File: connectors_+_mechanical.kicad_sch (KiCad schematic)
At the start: 6 parts, among them J1 Conn_01x06, J2 Conn_01x06, J3 Conn_01x04, Q1 BSP613P

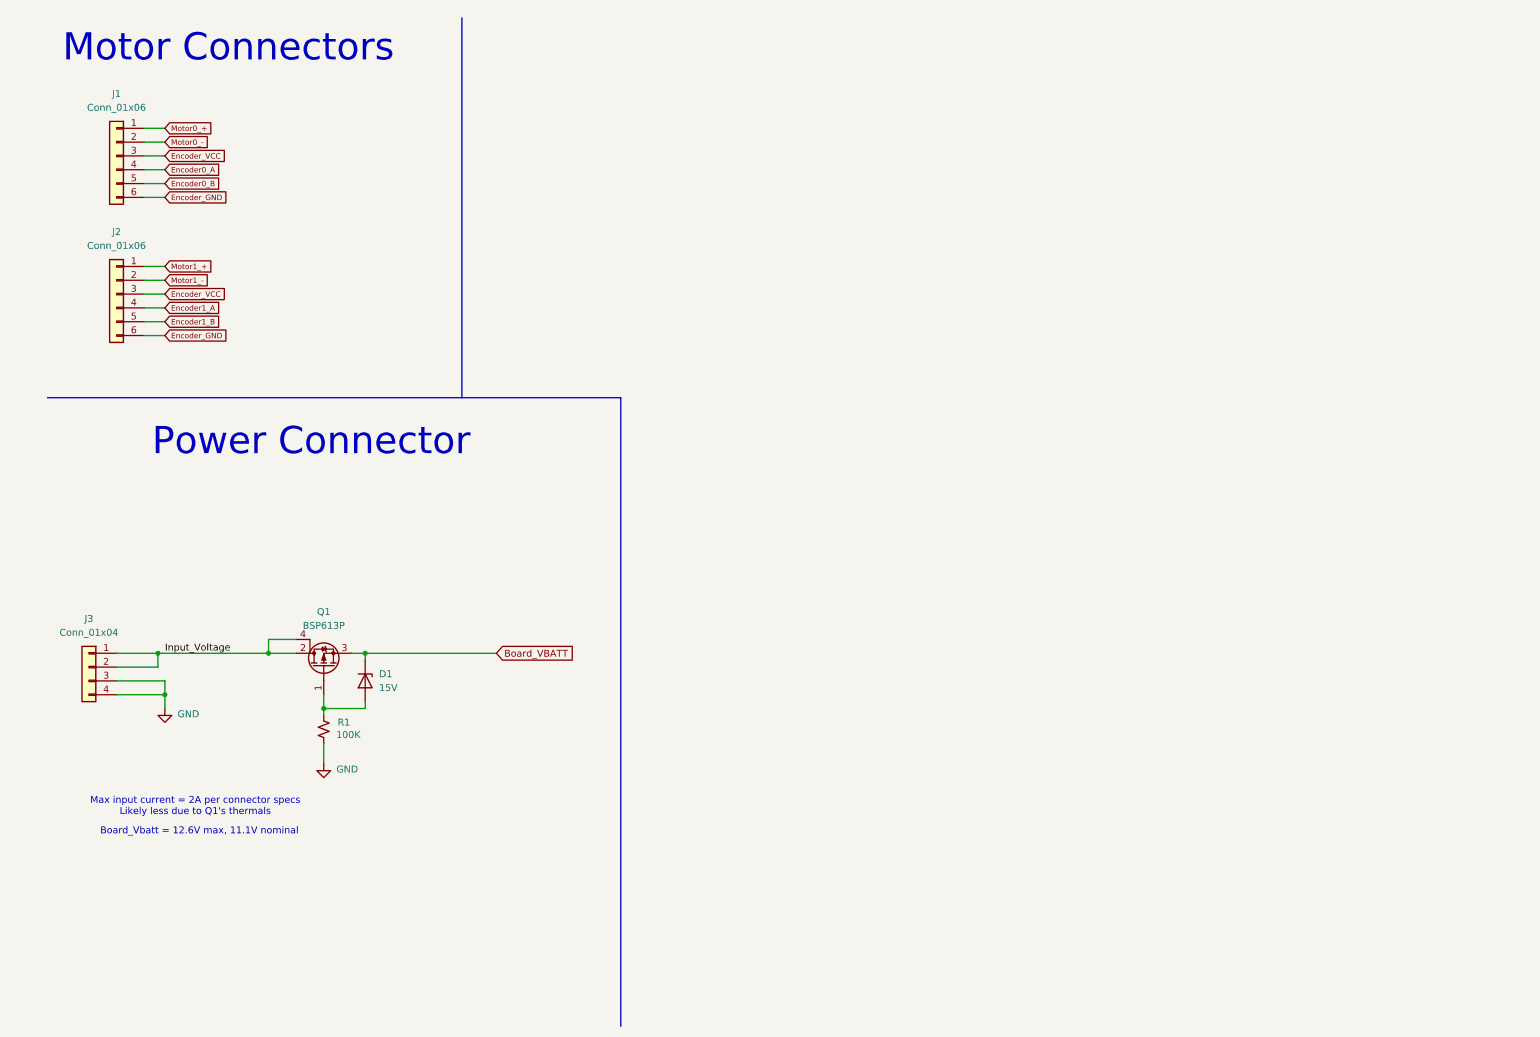
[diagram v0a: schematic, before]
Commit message: Added connectors
Added GPS and SD card connections
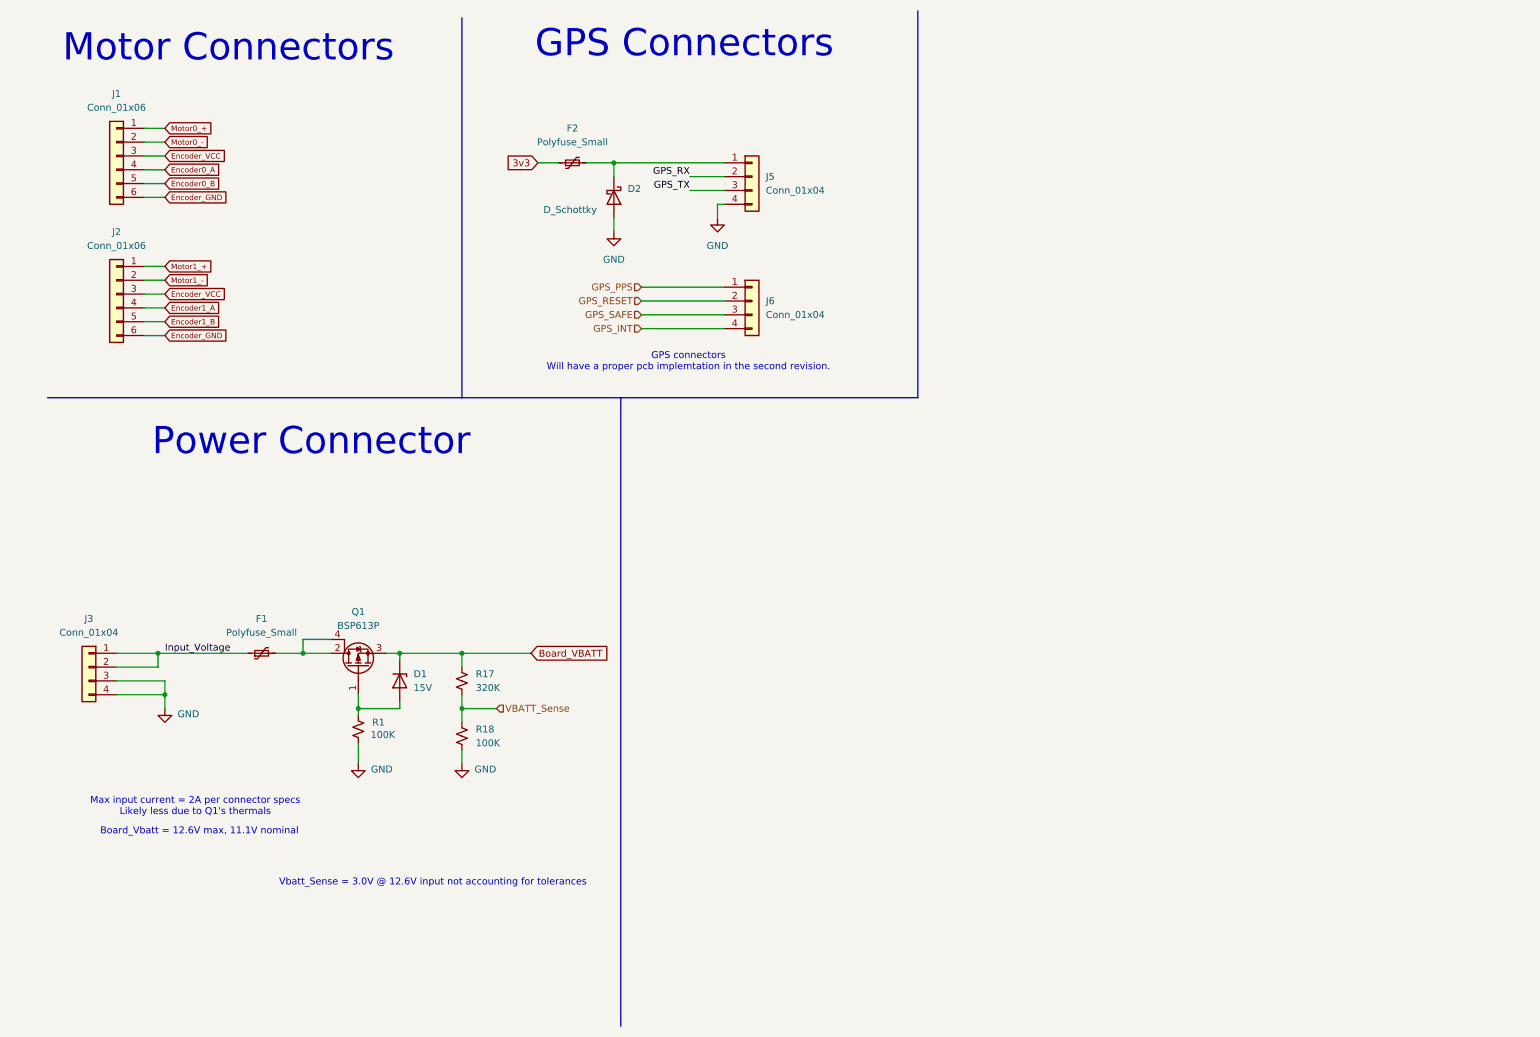
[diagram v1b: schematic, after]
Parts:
- added D2: D_Schottky, symbol Device:D_Schottky
- added F1, F2: Polyfuse_Small, symbol Device:Polyfuse_Small
- added J5, J6: Conn_01x04, symbol Connector_Generic:Conn_01x04
- added R17: 320K, symbol Device:R_Small_US
- added R18: 100K, symbol Device:R_Small_US
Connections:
- net Board_VBATT: now also R17.1
- net GND: now also D2.2 (A), J5.4 (Pin_4), R18.2
- net Input_Voltage: now also F1.1; no longer Q1.2 (D), Q1.4 (D)
- new net: D2.1 (K), F2.2, J5.1 (Pin_1)
- new net: F1.2, Q1.2 (D), Q1.4 (D)
- new net 3v3: F2.1
- new net GPS_INT: J6.4 (Pin_4)
- new net GPS_PPS: J6.1 (Pin_1)
- new net GPS_RESET: J6.2 (Pin_2)
- new net GPS_RX: J5.2 (Pin_2)
- new net GPS_SAFE: J6.3 (Pin_3)
- new net GPS_TX: J5.3 (Pin_3)
- new net VBATT_Sense: R17.2, R18.1
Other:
- note added: "GPS Connectors"
- note added: "GPS connectors Will have a proper pcb implemtation in the second revision."
- note added: "Vbatt_Sense = 3.0V @ 12.6V input not accounting for tolerances"
- moved on the sheet: D1, Q1, R1

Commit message: Updated schematics
Added the input current sense, expansion header and various test points.
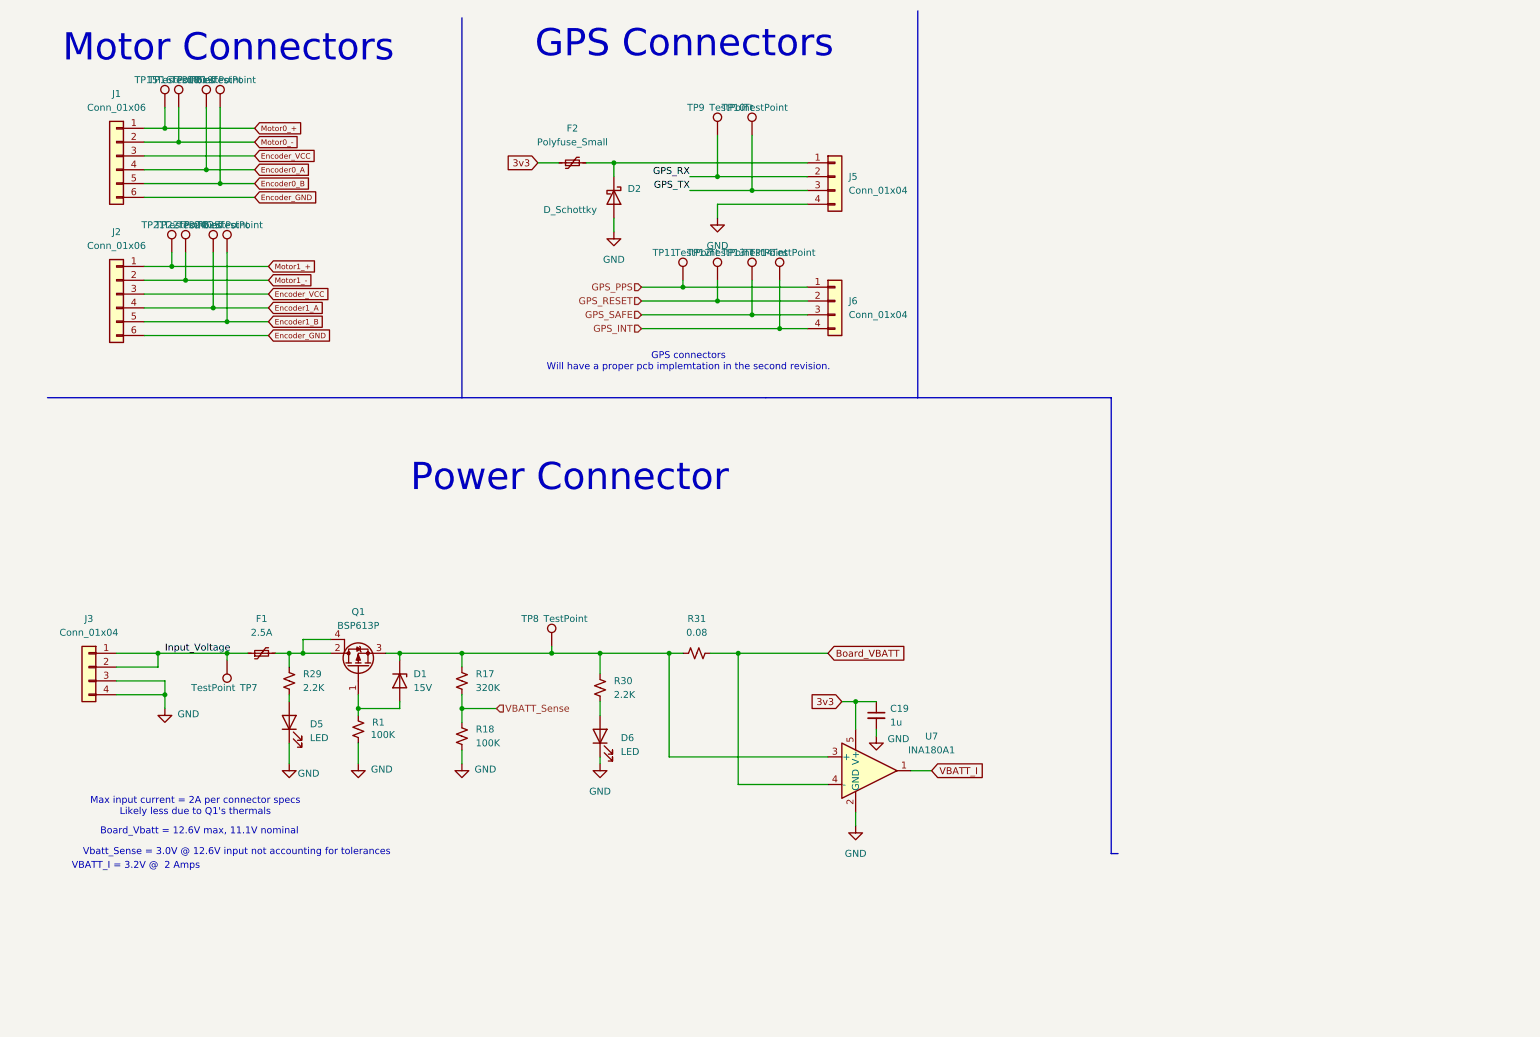
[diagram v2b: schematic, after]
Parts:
- added C19: 1u, symbol Device:C_Small
- added D5, D6: LED, symbol Device:LED
- added R29, R30: 2.2K, symbol Device:R_Small_US
- added R31: 0.08, symbol Device:R_Small_US
- added TP10, TP11, TP12, TP13, TP14, TP15, TP16, TP18, TP19, TP21, TP22, TP24, TP25, TP7, TP8, TP9: TestPoint, symbol Connector:TestPoint
- added U7: INA180A1, Package_TO_SOT_SMD:SOT-23-5, symbol Amplifier_Current:INA180A1
- F1: value Polyfuse_Small -> 2.5A
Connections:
- net 3v3: now also C19.1, U7.5 (V+)
- net Board_VBATT: now also R31.2, U7.4 (-); no longer D1.1 (K), Q1.3 (S), R17.1
- net Encoder0_A: now also TP18.1
- net Encoder0_B: now also TP19.1
- net Encoder1_A: now also TP24.1
- net Encoder1_B: now also TP25.1
- net GND: now also C19.2, D5.1 (K), D6.1 (K), U7.2 (GND)
- net GPS_INT: now also TP14.1
- net GPS_PPS: now also TP11.1
- net GPS_RESET: now also TP12.1
- net GPS_RX: now also TP9.1
- net GPS_SAFE: now also TP13.1
- net GPS_TX: now also TP10.1
- net Input_Voltage: now also TP7.1
- net Motor0_+: now also TP15.1
- net Motor0_-: now also TP16.1
- net Motor1_+: now also TP21.1
- net Motor1_-: now also TP22.1
- net at F1.2, Q1.2 (D), Q1.4 (D): now also R29.1
- new net: D1.1 (K), Q1.3 (S), R17.1, R30.1, R31.1, TP8.1, U7.3 (+)
- new net: D6.2 (A), R30.2
- new net: D5.2 (A), R29.2
- new net VBATT_I: U7.1
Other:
- note added: "VBATT_I = 3.2V @ 2 Amps"
- moved on the sheet: J5, J6

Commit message: Setup top sheet
Added TVS diodes, updated top sheet, misc label fixes
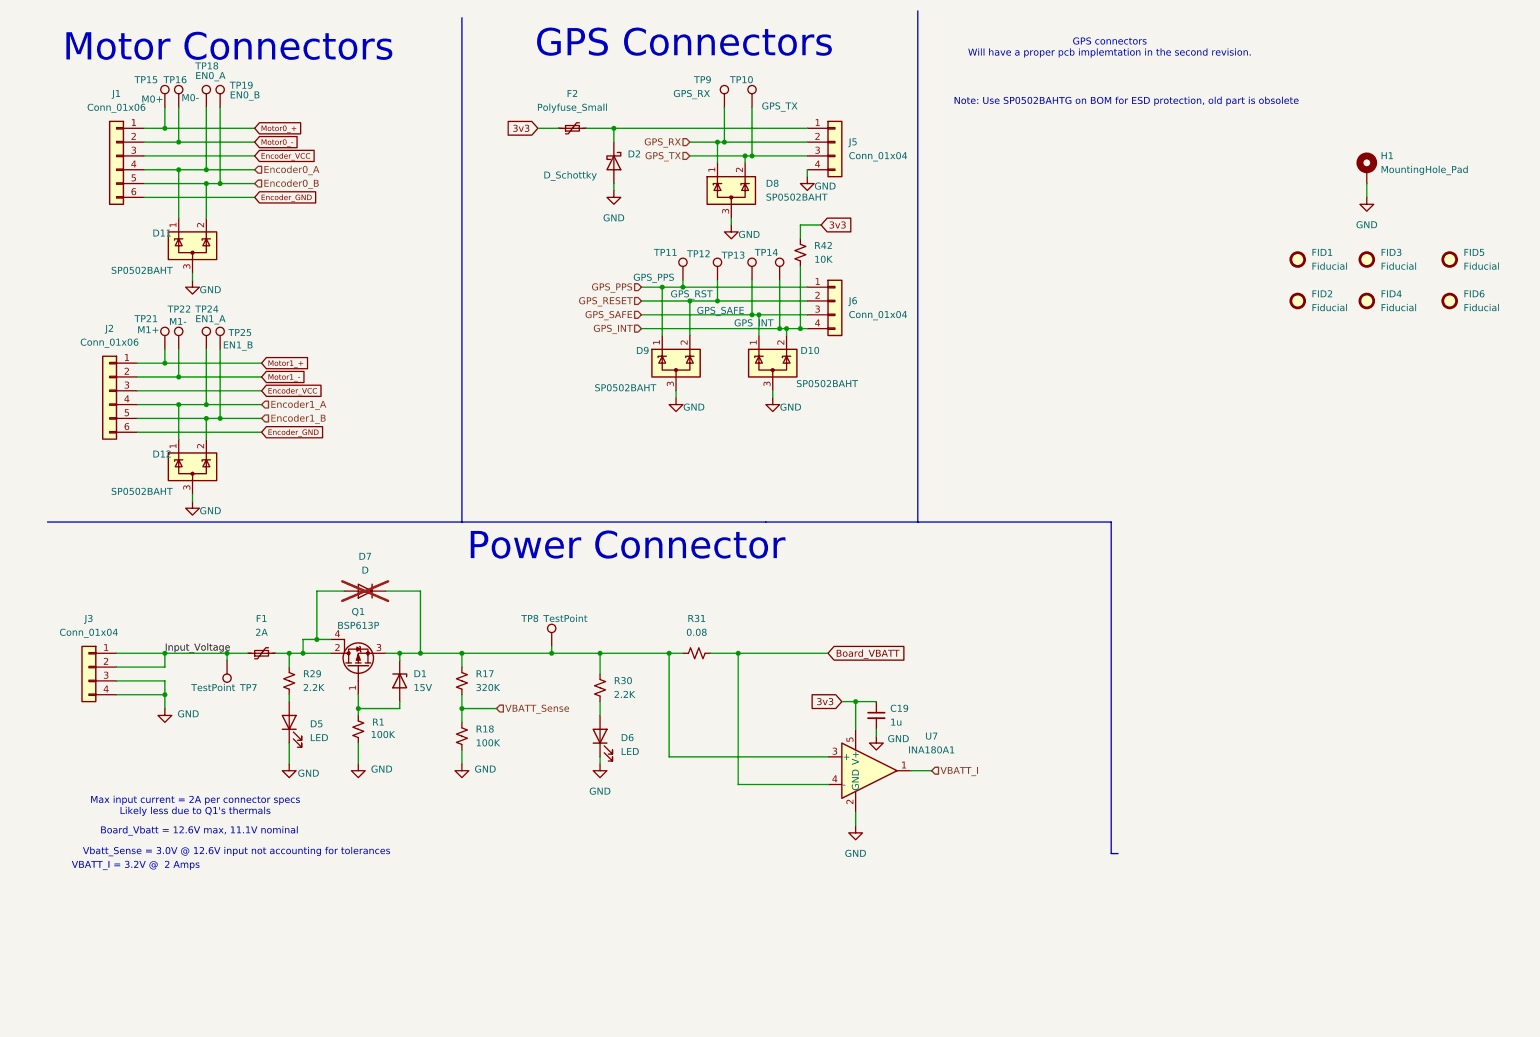
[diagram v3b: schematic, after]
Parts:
- added D10, D11, D12, D8, D9: SP0502BAHT, Package_TO_SOT_SMD:SOT-23, symbol Power_Protection:SP0502BAHT
- added D7: D, symbol Device:D
- added FID1, FID2, FID3, FID4, FID5, FID6: Fiducial, symbol Mechanical:Fiducial
- added H1: MountingHole_Pad, symbol Mechanical:MountingHole_Pad
- added R42: 10K, symbol Device:R_Small_US
- F1: value 2.5A -> 2A
- TP10: value TestPoint -> GPS_TX
- TP11: value TestPoint -> GPS_PPS
- TP12: value TestPoint -> GPS_RST
- TP13: value TestPoint -> GPS_SAFE
- TP14: value TestPoint -> GPS_INT
- TP15: value TestPoint -> M0+
- TP16: value TestPoint -> M0-
- TP18: value TestPoint -> EN0_A
- TP19: value TestPoint -> EN0_B
- TP21: value TestPoint -> M1+
- TP22: value TestPoint -> M1-
- TP24: value TestPoint -> EN1_A
- TP25: value TestPoint -> EN1_B
- TP9: value TestPoint -> GPS_RX
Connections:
- net 3v3: now also R42.1
- net Encoder0_A: now also D11.1 (K)
- net Encoder0_B: now also D11.2 (K)
- net Encoder1_A: now also D12.1 (K)
- net Encoder1_B: now also D12.2 (K)
- net GND: now also D10.3 (A), D11.3 (A), D12.3 (A), D8.3 (A), D9.3 (A), H1.1
- net GPS_INT: now also D10.2 (K), R42.2
- net GPS_PPS: now also D9.1 (K)
- net GPS_RESET: now also D9.2 (K)
- net GPS_RX: now also D8.1 (K)
- net GPS_SAFE: now also D10.1 (K)
- net GPS_TX: now also D8.2 (K)
- net at D1.1 (K), Q1.3 (S), R17.1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: now also D7.1 (K)
- net at F1.2, Q1.2 (D), Q1.4 (D)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: now also D7.2 (A)
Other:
- note added: "Note: Use SP0502BAHTG on BOM for ESD protection, old part is obsolete"
- moved on the sheet: D2, F2, J2, J5, TP10, TP21, TP22, TP24, TP25, TP9

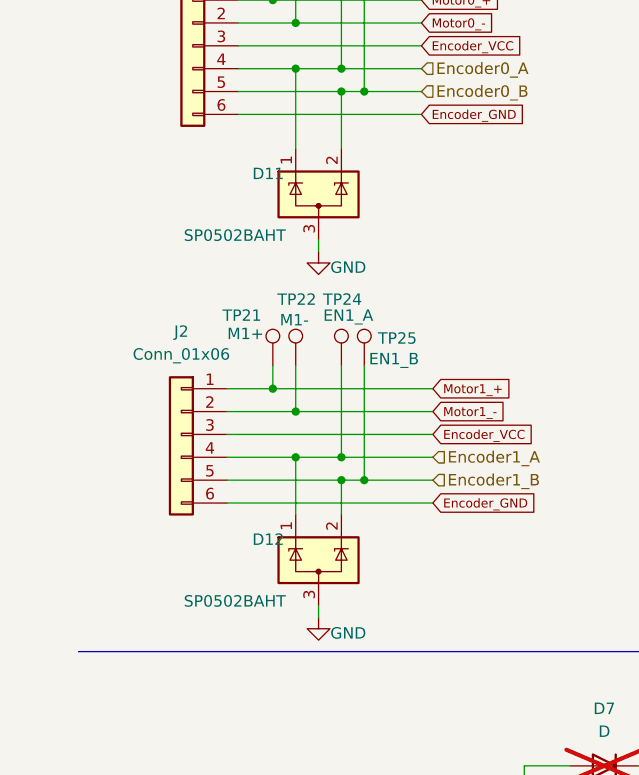
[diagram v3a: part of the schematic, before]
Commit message: Updated MCU pinout
Added bypass caps and started assigning pinouts.
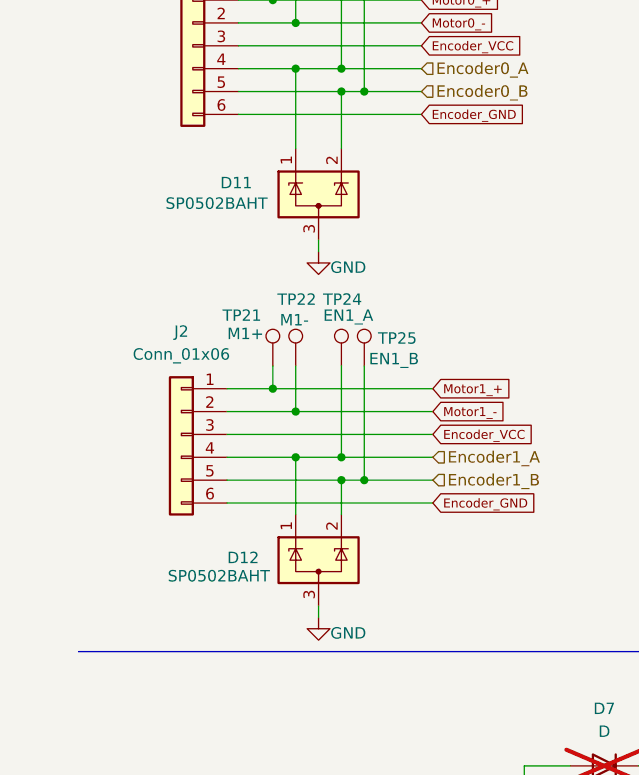
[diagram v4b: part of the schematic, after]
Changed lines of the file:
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@@
 		(dnp no)
 		(property "Reference" "D12"
-			(at 32.004 92.964 0)
+			(at 29.21 94.996 0)
 			(effects
 				(font
@@
 		)
 		(property "Value" "SP0502BAHT"
-			(at 24.384 99.822 0)
+			(at 22.606 97.028 0)
 			(effects
 				(font
@@
 		(dnp no)
 		(property "Reference" "D11"
-			(at 32.004 52.324 0)
+			(at 28.448 53.34 0)
 			(effects
 				(font
@@
 		)
 		(property "Value" "SP0502BAHT"
-			(at 24.384 59.182 0)
-			(effects
-				(font
+			(at 22.352 55.626 0)
+			(effects
+				(font
